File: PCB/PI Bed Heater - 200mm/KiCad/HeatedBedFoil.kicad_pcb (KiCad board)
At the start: 2 copper layers, 200 x 200 mm, 7 parts, among them J1 Screw_Terminal_01x01

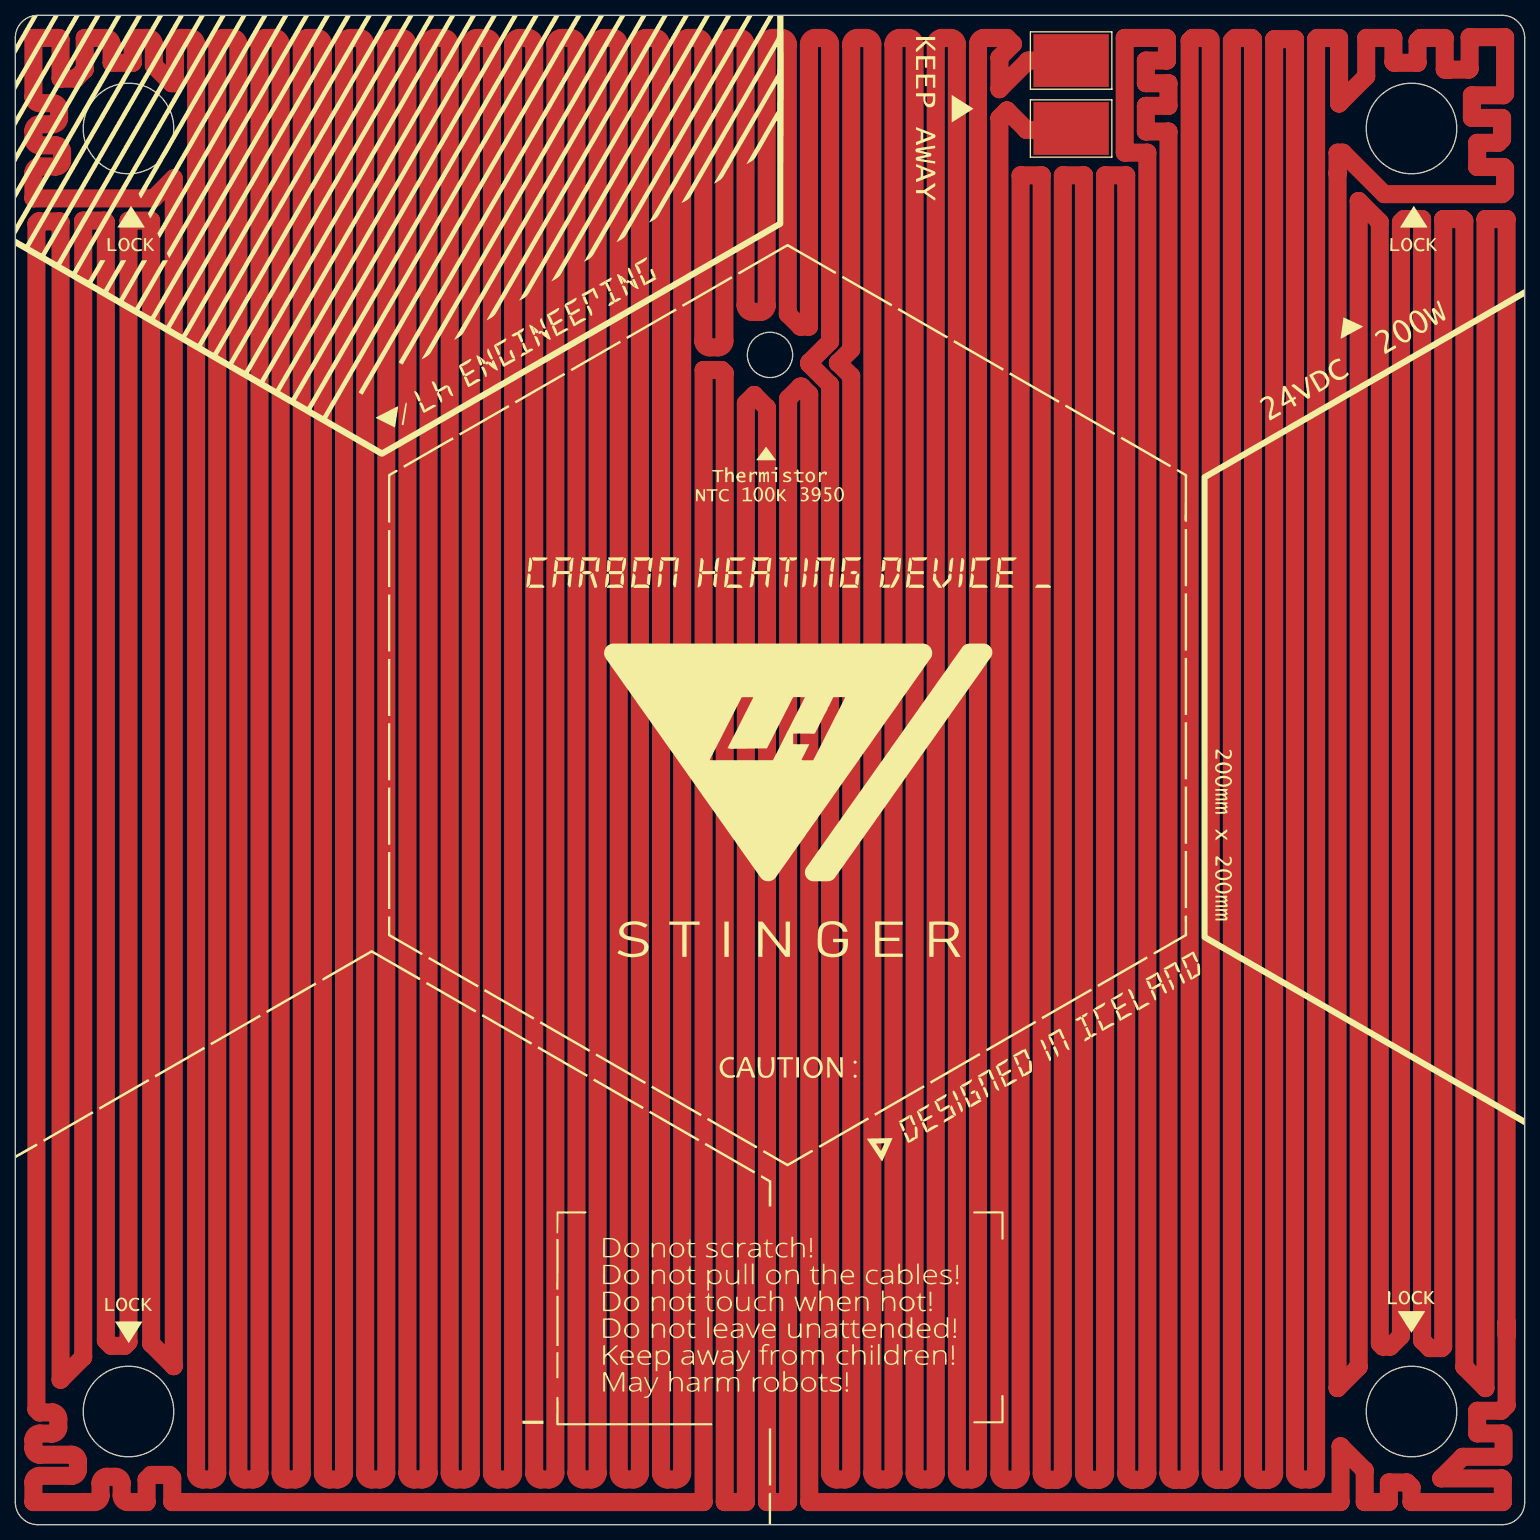
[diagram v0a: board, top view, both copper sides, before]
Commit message: updating polyimide heater pcb
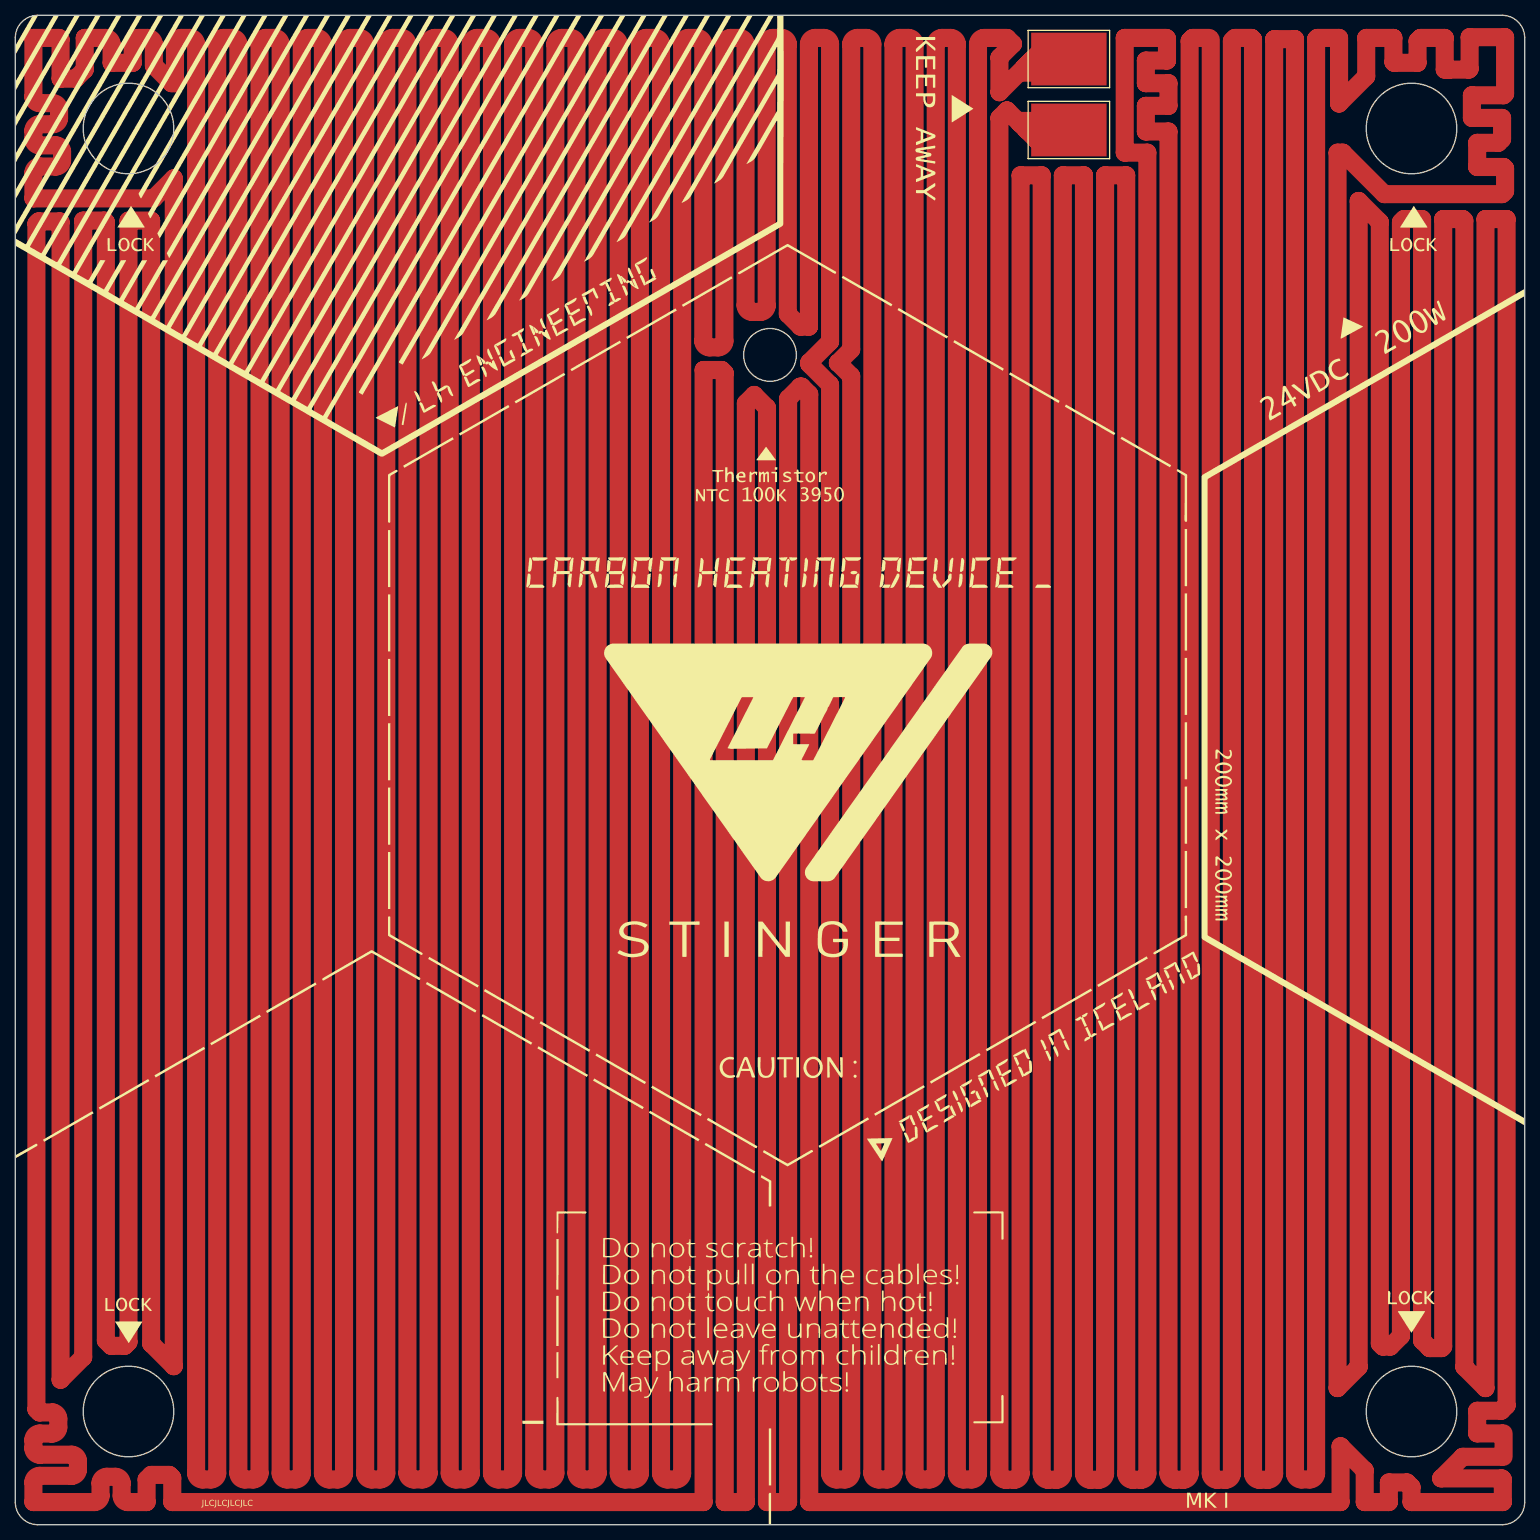
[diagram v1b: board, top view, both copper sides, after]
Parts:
- removed H1 (x3), H2, H5: MountingHole, MountingHole:MountingHole_5.5mm
- moved J1 0.36 mm to (179.6, 45.8)
- moved J1 0.36 mm to (179.6, 55.2)
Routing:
- net Net-(F1-Pad1): track 13318.5 -> 13341.3 mm
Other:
- outline, holes or cut-outs redrawn
- board text added: "JLCJLCJLCJLC"
- board text added: "MK I"

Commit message: Updating Flex Stiffener information.
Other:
- board text added: "27 x 22 x 0.2 mm"
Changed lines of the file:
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@@
     (effects (font (size 2 2) (thickness 0.15)) (justify left bottom))
+  )
+  (gr_text "27 x 22 x 0.2 mm " (at 180.7 78.7) (layer "User.1")
+    (effects (font (size 3 3) (thickness 0.15)) (justify left bottom))
+  )
+  (dimension (type aligned) (layer "User.1")
+    (pts (xy 180.165 40.51) (xy 180.165 62.1))
+    (height -23.335)
+    (gr_text "22 mm" (at 201.35 51.305 90) (layer "User.1")
+      (effects (font (size 2 2) (thickness 0.15)))
+    )
+    (format (prefix "") (suffix "") (units 2) (units_format 1) (precision 4) (override_value "22") suppress_zeroes)
+    (style (thickness 0.15) (arrow_length 1.27) (text_position_mode 0) (extension_height 0.58642) (extension_offset 0.5) keep_text_aligned)
+  )
+  (dimension (type aligned) (layer "User.1")
+    (pts (xy 166.83 51.305) (xy 193.5 51.305))
+    (height -18.805)
+    (gr_text "27 mm" (at 180.165 30.35) (layer "User.1")
+      (effects (font (size 2 2) (thickness 0.15)))
+    )
+    (format (prefix "") (suffix "") (units 2) (units_format 1) (precision 4) (override_value "27") suppress_zeroes)
+    (style (thickness 0.15) (arrow_length 1.27) (text_position_mode 0) (extension_height 0.58642) (extension_offset 0.5) keep_text_aligned)
+  )
+  (dimension (type aligned) (layer "User.2")
+    (pts (xy 240 150.1) (xy 40.3 150.1))
+    (height 125.7)
+    (gr_text "200 mm" (at 140.15 21.25) (layer "User.2")
+      (effects (font (size 3 3) (thickness 0.15)))
+    )
+    (format (prefix "") (suffix "") (units 2) (units_format 1) (precision 4) (override_value "200") suppress_zeroes)
+    (style (thickness 0.15) (arrow_length 1.27) (text_position_mode 0) (extension_height 0.58642) (extension_offset 0.5) keep_text_aligned)
+  )
+  (dimension (type aligned) (layer "User.2")
+    (pts (xy 140 40) (xy 140 240))
+    (height -185.1)
+    (gr_text "200 mm" (at 321.95 140 90) (layer "User.2")
+      (effects (font (size 3 3) (thickness 0.15)))
+    )
+    (format (prefix "") (suffix "") (units 2) (units_format 1) (precision 4) suppress_zeroes)
+    (style (thickness 0.15) (arrow_length 1.27) (text_position_mode 0) (extension_height 0.58642) (extension_offset 0.5) keep_text_aligned)
   )
   (dimension (type leader) (layer "User.1")
@@
   (dimension (type leader) (layer "User.2")
     (pts (xy 252.7 88) (xy 280 88))
-    (gr_text "3M Adhesive" (at 292.7 88) (layer "User.2")
+    (gr_text "3M468 (0.13mm) Adhesive" (at 292.7 88) (layer "User.2")
       (effects (font (size 3 3) (thickness 0.5)))
     )
-    (format (prefix "") (suffix "") (units 0) (units_format 0) (precision 4) (override_value "3M Adhesive"))
+    (format (prefix "") (suffix "") (units 0) (units_format 0) (precision 4) (override_value "3M468 (0.13mm) Adhesive"))
     (style (thickness 0.5) (arrow_length 1.27) (text_position_mode 0) (text_frame 0) (extension_offset 0.5))
   )

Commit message: updating instructions
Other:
- board text added: "200 x 200 x 0.13 mm"
- board text added: "Backside / Bottom Layer"
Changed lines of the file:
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@@
     (46 "B.CrtYd" user "B.Courtyard")
     (47 "F.CrtYd" user "F.Courtyard")
-    (50 "User.1" user "Stiffener Polyimide")
-    (51 "User.2" user "Stiffener 3M Adhesive")
+    (50 "User.1" user "B.Stiffener Polyimide")
+    (51 "User.2" user "B.Stiffener 3M Adhesive")
   )
   (setup
@@
   )
   (gr_text "27 x 22 x 0.2 mm " (at 180.7 78.7) (layer "User.1")
-    (effects (font (size 3 3) (thickness 0.15)) (justify left bottom))
+    (effects (font (size 3 3) (thickness 0.6) bold) (justify left bottom))
+  )
+  (gr_text "Backside / Bottom Layer" (at 161 99.1) (layer "User.1")
+    (effects (font (size 3 3) (thickness 0.5) bold) (justify left bottom))
+  )
+  (gr_text "Backside / Bottom Layer" (at 254.3 114.2) (layer "User.2")
+    (effects (font (size 3 3) (thickness 0.5) bold) (justify left bottom))
+  )
+  (gr_text "200 x 200 x 0.13 mm" (at 268.1 97.6) (layer "User.2")
+    (effects (font (size 3 3) (thickness 0.5) bold) (justify left bottom))
   )
   (dimension (type aligned) (layer "User.1")
@@
   )
   (dimension (type leader) (layer "User.2")
-    (pts (xy 252.7 88) (xy 280 88))
-    (gr_text "3M468 (0.13mm) Adhesive" (at 292.7 88) (layer "User.2")
+    (pts (xy 244.8 87.5) (xy 272.1 87.5))
+    (gr_text "3M468 Adhesive" (at 284.8 87.5) (layer "User.2")
       (effects (font (size 3 3) (thickness 0.5)))
     )
-    (format (prefix "") (suffix "") (units 0) (units_format 0) (precision 4) (override_value "3M468 (0.13mm) Adhesive"))
+    (format (prefix "") (suffix "") (units 0) (units_format 0) (precision 4) (override_value "3M468 Adhesive"))
     (style (thickness 0.5) (arrow_length 1.27) (text_position_mode 0) (text_frame 0) (extension_offset 0.5))
   )
